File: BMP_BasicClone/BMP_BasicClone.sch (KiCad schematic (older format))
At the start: 53 parts, among them J1 BARREL_JACK, Q1 MMBT3904, Q2 MMBT3904, Q3 MMBT3904, Q4 MMBT3904

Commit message: update
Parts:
- J1: symbol BARREL_JACK -> BARREL_JACK-RESCUE-BMP_BasicClone
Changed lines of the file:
@@
 EESchema Schematic File Version 2
+LIBS:BMP_BasicClone-rescue
 LIBS:power
 LIBS:device
@@
 VOLUME
 $Comp
-L BARREL_JACK J1
+L BARREL_JACK-RESCUE-BMP_BasicClone J1
 U 1 1 5A2DF800
 P 1650 1850

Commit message: updates
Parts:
- R1: value R -> 1k
- SW_EN1: footprint custom_sw:SW_3PDT_W18MM_L17.3MM_P5.3MM_D2MM -> custom_sw:SW_3PDT_W18MM_L17.3MM_P5.3MM_D2MM_SolderLugs
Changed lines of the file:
@@
 F 0 "SW_EN1" H 9850 2700 50  0000 C CNN
 F 1 "SW_3PDT_on_on" H 9800 2750 50  0001 C CNN
-F 2 "custom_sw:SW_3PDT_W18MM_L17.3MM_P5.3MM_D2MM" H 9800 2950 50  0001 C CNN
+F 2 "custom_sw:SW_3PDT_W18MM_L17.3MM_P5.3MM_D2MM_SolderLugs" H 9800 2950 50  0001 C CNN
 F 3 "" H 9800 2950 50  0001 C CNN
 	1    9800 2950
@@
 F 0 "SW_EN1" H 1700 2800 50  0000 C CNN
 F 1 "SW_3PDT_on_on" H 1700 2800 50  0001 C CNN
-F 2 "custom_sw:SW_3PDT_W18MM_L17.3MM_P5.3MM_D2MM" H 1700 3000 50  0001 C CNN
+F 2 "custom_sw:SW_3PDT_W18MM_L17.3MM_P5.3MM_D2MM_SolderLugs" H 1700 3000 50  0001 C CNN
 F 3 "" H 1700 3000 50  0001 C CNN
 	2    1700 3000
@@
 F 0 "SW_EN1" H 1950 6000 50  0000 C CNN
 F 1 "SW_3PDT_on_on" H 1950 6000 50  0001 C CNN
-F 2 "custom_sw:SW_3PDT_W18MM_L17.3MM_P5.3MM_D2MM" H 1950 6200 50  0001 C CNN
+F 2 "custom_sw:SW_3PDT_W18MM_L17.3MM_P5.3MM_D2MM_SolderLugs" H 1950 6200 50  0001 C CNN
 F 3 "" H 1950 6200 50  0001 C CNN
 	3    1950 6200
@@
 P 2850 2900
 F 0 "R1" V 2930 2900 50  0000 C CNN
-F 1 "R" V 2850 2900 50  0000 C CNN
+F 1 "1k" V 2850 2900 50  0000 C CNN
 F 2 "Resistors_SMD:R_0402_NoSilk" V 2780 2900 50  0001 C CNN
 F 3 "" H 2850 2900 50  0001 C CNN

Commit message: update
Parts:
- removed R24, R25, R26: 100K, Potentiometers:Potentiometer_Bourns_PTV09A-1_Horizontal, symbol POT
- added J2, J3: CONN_02X06, Pin_Headers:Pin_Header_Straight_2x06_Pitch2.54mm, symbol CONN_02X06
- added SUSTAIN1, TONE1, VOLUME1: 100K, Potentiometers:Potentiometer_Bourns_PTV09A-1_Horizontal, symbol POT
- C1, C10, C11, C12, C13, C2, C3, C4, C5, C6, C7, C8, C9: footprint Capacitors_SMD:C_0402_NoSilk -> Capacitors_SMD:C_0805
- D1, D2, D3, D4, D6: footprint Diodes_SMD:D_SOD-323_HandSoldering -> Diodes_SMD:D_SOD-523
- R1, R10, R11, R12, R13, R14, R15, R16, R17, R18, R19, R2, R20, R21, R22, R23, R3, R4, R5, R6, R7, R8, R9: footprint Resistors_SMD:R_0402_NoSilk -> Resistors_SMD:R_0805
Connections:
- net GND: now also J2.2 (P2), J2.8 (P8); no longer R1.1
- net SUS_P3: now reaches C4.1
- net SUS_P3: now also J2.7 (P7)
- net SUS_P2: now reaches C5.1
- net SUS_P2: now also J2.9 (P9)
- net SUS_P1: now reaches R23.1
- net SUS_P1: now also J2.11 (P11)
- net TONE_P3: now reaches C9.1, R5.2
- net TONE_P3: now also J2.1 (P1)
- net TONE_P1: now reaches C8.1, R8.1
- net TONE_P1: now also J2.5 (P5)
- net TONE_P2: now reaches C3.2
- net TONE_P2: now also J2.3 (P3)
- net VOL_P1: now reaches C2.2
- net VOL_P1: now also J2.12 (P12)
- net VOL_P2: now reaches SW_EN1.3 (C)
- net VOL_P2: now also J2.10 (P10)
- net at D5.2 (A): now also J3.4 (P4); no longer SW_EN1.6 (C)
- net at D5.1 (K): now also R1.1; no longer R1.2
- new net: J3.2 (P2), R1.2
- new net: J3.1 (P1), TONE1.1
- new net: J3.10 (P10), VOLUME1.2
- new net: J3.11 (P11), SUSTAIN1.3
- new net: J3.12 (P12), VOLUME1.1
- new net: J3.3 (P3), TONE1.2
- new net: J3.5 (P5), TONE1.3
- new net: J3.7 (P7), SUSTAIN1.1
- new net: J3.8 (P8), VOLUME1.3
- new net: J3.9 (P9), SUSTAIN1.2
- new net LED_AN: J2.4 (P4), SW_EN1.6 (C)
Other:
- note removed: "SUSTAIN"
- note removed: "TONE"
- note removed: "VOLUME"
- moved on the sheet: C1, C10, C11, C12, C13, C2, C3, C4, C5, C6, C7, C8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

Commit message: board update
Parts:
- renumbered C9 to C10, C8 to C11, C3 to C12, C2 to C13, C10 to C2, C4 to C3, C5 to C4, C6 to C5, C12 to C6, C13 to C7, C7 to C8, C11 to C9, D6 to D1, D4 to D2, D2 to D4, D1 to D5, D5 to D6, Q4 to Q1, Q3 to Q2, Q2 to Q3, Q1 to Q4, R2 to R1, R18 to R10, R21 to R11, R16 to R13, R15 to R14, R11 to R15, R10 to R16, R8 to R17, R5 to R18, R7 to R19, R14 to R2, R3 to R20, R6 to R21, R4 to R22, R1 to R23, R9 to R3, R13 to R4, R22 to R5, R23 to R6, R19 to R7, R20 to R8, R17 to R9
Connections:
- net +9V: now also SW_EN1.5 (B); no longer SW_EN1.5 (B)
- net LED_AN: now also SW_EN1.6 (C); no longer SW_EN1.6 (C)
- net VOL_P2: now also SW_EN1.1 (A); no longer SW_EN1.3 (C)
- net at R1.2: now also SW_EN1.7 (A); no longer SW_EN1.9 (C)
- net at J_OUT1.1 (TIP): now also SW_EN1.2 (B); no longer SW_EN1.2 (B)
- net at J_IN1.1 (TIP): now also SW_EN1.8 (B); no longer SW_EN1.8 (B)
- new net: SW_EN1.3 (C), SW_EN1.9 (C)

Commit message: Update
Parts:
- removed J2, J3: CONN_02X06, Pin_Headers:Pin_Header_Straight_2x06_Pitch2.54mm, symbol CONN_02X06
- added J_AUX2MAIN_1, J_AUX2MAIN_2, J_MAIN2AUX_1, J_MAIN2AUX_2: CONN_01X06, Pin_Headers:Pin_Header_Straight_1x06_Pitch2.54mm, symbol CONN_01X06
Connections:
- net GND: now also J_MAIN2AUX_2.3 (P3), J_MAIN2AUX_2.6 (P6)
- net LED_AN: now also J_MAIN2AUX_2.5 (P5)
- net SUS_P1: now also J_MAIN2AUX_1.6 (P6)
- net SUS_P2: now also J_MAIN2AUX_1.5 (P5)
- net SUS_P3: now also J_MAIN2AUX_1.4 (P4)
- net TONE_P1: now also J_MAIN2AUX_1.3 (P3)
- net TONE_P2: now also J_MAIN2AUX_1.2 (P2)
- net TONE_P3: now also J_MAIN2AUX_1.1 (P1)
- net VOL_P1: now also J_MAIN2AUX_2.1 (P1)
- net VOL_P2: now also J_MAIN2AUX_2.2 (P2)
- net at D6.2 (A): now also J_AUX2MAIN_2.5 (P5)
- net at R23.2: now also J_AUX2MAIN_2.6 (P6)
- net at TONE1.1: now also J_AUX2MAIN_1.1 (P1)
- net at VOLUME1.2: now also J_AUX2MAIN_2.2 (P2)
- net at SUSTAIN1.3: now also J_AUX2MAIN_1.6 (P6)
- net at VOLUME1.1: now also J_AUX2MAIN_2.1 (P1)
- net at TONE1.2: now also J_AUX2MAIN_1.2 (P2)
- net at TONE1.3: now also J_AUX2MAIN_1.3 (P3)
- net at SUSTAIN1.1: now also J_AUX2MAIN_1.4 (P4)
- net at VOLUME1.3: now also J_AUX2MAIN_2.3 (P3)
- net at SUSTAIN1.2: now also J_AUX2MAIN_1.5 (P5)
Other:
- moved on the sheet: D6, R23, SUSTAIN1, TONE1, VOLUME1
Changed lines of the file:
@@
 L LED D6
 U 1 1 5A2E0726
-P 9200 5750
-F 0 "D6" H 9200 5850 50  0000 C CNN
-F 1 "LED" H 9200 5650 50  0000 C CNN
-F 2 "LEDs:LED_D5.0mm" H 9200 5750 50  0001 C CNN
-F 3 "" H 9200 5750 50  0001 C CNN
-	1    9200 5750
+P 9200 5850
+F 0 "D6" H 9200 5950 50  0000 C CNN
+F 1 "LED" H 9200 5750 50  0000 C CNN
+F 2 "LEDs:LED_D5.0mm" H 9200 5850 50  0001 C CNN
+F 3 "" H 9200 5850 50  0001 C CNN
+	1    9200 5850
 	0    -1   -1   0
 $EndComp
@@
 L R R23
 U 1 1 5A2E81A3
-P 9500 5750
-F 0 "R23" V 9580 5750 50  0000 C CNN
-F 1 "1k" V 9500 5750 50  0000 C CNN
-F 2 "Resistors_SMD:R_0805" V 9430 5750 50  0001 C CNN
-F 3 "" H 9500 5750 50  0001 C CNN
-	1    9500 5750
+P 9500 5850
+F 0 "R23" V 9580 5850 50  0000 C CNN
+F 1 "1k" V 9500 5850 50  0000 C CNN
+F 2 "Resistors_SMD:R_0805" V 9430 5850 50  0001 C CNN
+F 3 "" H 9500 5850 50  0001 C CNN
+	1    9500 5850
 	-1   0    0    1
 $EndComp
@@
 $EndComp
 $Comp
-L CONN_02X06 J3
-U 1 1 5A33F471
-P 9050 5200
-F 0 "J3" H 9050 5550 50  0000 C CNN
-F 1 "CONN_02X06" H 9050 4850 50  0000 C CNN
-F 2 "Pin_Headers:Pin_Header_Straight_2x06_Pitch2.54mm" H 9050 4000 50  0001 C CNN
-F 3 "" H 9050 4000 50  0001 C CNN
-	1    9050 5200
-	0    1    1    0
-$EndComp
-$Comp
 L POT SUSTAIN1
 U 1 1 5A34007A
-P 8750 4350
-F 0 "SUSTAIN1" V 8550 4350 50  0000 C CNN
-F 1 "100K" V 8650 4350 50  0000 C CNN
-F 2 "Potentiometers:Potentiometer_Bourns_PTV09A-1_Horizontal" H 8750 4350 50  0001 C CNN
-F 3 "" H 8750 4350 50  0001 C CNN
-	1    8750 4350
+P 8750 4200
+F 0 "SUSTAIN1" V 8550 4200 50  0000 C CNN
+F 1 "100K" V 8650 4200 50  0000 C CNN
+F 2 "Potentiometers:Potentiometer_Bourns_PTV09A-1_Horizontal" H 8750 4200 50  0001 C CNN
+F 3 "" H 8750 4200 50  0001 C CNN
+	1    8750 4200
 	0    1    1    0
 $EndComp
@@
 Text Label 4250 5400 1    60   ~ 0
 SUS_P2
-$Comp
-L CONN_02X06 J2
-U 1 1 5A342A65
-P 8050 5200
-F 0 "J2" H 8050 5550 50  0000 C CNN
-F 1 "CONN_02X06" H 8050 4850 50  0000 C CNN
-F 2 "Pin_Headers:Pin_Header_Straight_2x06_Pitch2.54mm" H 8050 4000 50  0001 C CNN
-F 3 "" H 8050 4000 50  0001 C CNN
-	1    8050 5200
-	0    1    1    0
-$EndComp
-Text Label 7800 4550 3    60   ~ 0
+Text Label 7650 4400 3    60   ~ 0
 SUS_P1
-Text Label 7900 4550 3    60   ~ 0
+Text Label 7750 4400 3    60   ~ 0
 SUS_P2
-Text Label 8000 4550 3    60   ~ 0
+Text Label 7850 4400 3    60   ~ 0
 SUS_P3
 $Comp
 L POT TONE1
 U 1 1 5A3434FD
-P 9350 4350
-F 0 "TONE1" V 9150 4350 50  0000 C CNN
-F 1 "100K" V 9250 4350 50  0000 C CNN
-F 2 "Potentiometers:Potentiometer_Bourns_PTV09A-1_Horizontal" H 9350 4350 50  0001 C CNN
-F 3 "" H 9350 4350 50  0001 C CNN
-	1    9350 4350
+P 9350 4200
+F 0 "TONE1" V 9150 4200 50  0000 C CNN
+F 1 "100K" V 9250 4200 50  0000 C CNN
+F 2 "Potentiometers:Potentiometer_Bourns_PTV09A-1_Horizontal" H 9350 4200 50  0001 C CNN
+F 3 "" H 9350 4200 50  0001 C CNN
+	1    9350 4200
 	0    1    1    0
 $EndComp
-Text Label 8100 4550 3    60   ~ 0
+Text Label 7950 4400 3    60   ~ 0
 TONE_P1
-Text Label 8200 4550 3    60   ~ 0
+Text Label 8050 4400 3    60   ~ 0
 TONE_P2
-Text Label 8300 4550 3    60   ~ 0
+Text Label 8150 4400 3    60   ~ 0
 TONE_P3
 Text Label 7550 2400 3    60   ~ 0
@@
 Text Label 7400 2250 0    60   ~ 0
 TONE_P2
-Text Label 7800 5850 1    60   ~ 0
+Text Label 7650 5950 1    60   ~ 0
 VOL_P1
-Text Label 7900 5850 1    60   ~ 0
+Text Label 7750 5950 1    60   ~ 0
 VOL_P2
-Text Label 8000 5850 1    60   ~ 0
+Text Label 7850 5950 1    60   ~ 0
 VOL_P3
-Text Label 8200 5850 1    60   ~ 0
+Text Label 8050 5950 1    60   ~ 0
 LED_AN
-Text Label 8300 5850 1    60   ~ 0
+Text Label 8150 5950 1    60   ~ 0
 LED_CA
 $Comp
 L POT VOLUME1
 U 1 1 5A346136
-P 8750 6000
-F 0 "VOLUME1" V 8550 6000 50  0000 C CNN
-F 1 "100K" V 8650 6000 50  0000 C CNN
-F 2 "Potentiometers:Potentiometer_Bourns_PTV09A-1_Horizontal" H 8750 6000 50  0001 C CNN
-F 3 "" H 8750 6000 50  0001 C CNN
-	1    8750 6000
+P 8750 6100
+F 0 "VOLUME1" V 8550 6100 50  0000 C CNN
+F 1 "100K" V 8650 6100 50  0000 C CNN
+F 2 "Potentiometers:Potentiometer_Bourns_PTV09A-1_Horizontal" H 8750 6100 50  0001 C CNN
+F 3 "" H 8750 6100 50  0001 C CNN
+	1    8750 6100
 	0    -1   -1   0
 $EndComp
@@
 VOL_P3
 Wire Wire Line
-	9300 5500 9300 5450
-Wire Wire Line
-	9500 5500 9300 5500
-Wire Wire Line
-	9500 5600 9500 5500
-Wire Wire Line
-	9500 6050 9500 5900
-Wire Wire Line
-	9200 6050 9500 6050
-Wire Wire Line
-	9200 5900 9200 6050
-Wire Wire Line
-	9200 5600 9200 5450
-Wire Wire Line
-	8800 5550 8800 5450
-Wire Wire Line
-	8550 5550 8800 5550
-Wire Wire Line
-	8550 6000 8550 5550
-Wire Wire Line
-	8600 6000 8550 6000
-Wire Wire Line
-	8900 5650 8900 5450
-Wire Wire Line
-	8750 5650 8900 5650
-Wire Wire Line
-	8750 5850 8750 5650
-Wire Wire Line
-	9000 6000 9000 5450
-Wire Wire Line
-	8900 6000 9000 6000
-Wire Wire Line
-	8200 5450 8200 5850
-Wire Wire Line
-	8300 5450 8300 5850
-Wire Wire Line
-	8000 5450 8000 5850
-Wire Wire Line
-	7900 5450 7900 5850
-Wire Wire Line
-	7800 5450 7800 5850
-Wire Wire Line
-	8300 4950 8300 4550
-Wire Wire Line
-	8200 4550 8200 4950
-Wire Wire Line
-	8100 4550 8100 4950
-Wire Wire Line
-	9550 4350 9500 4350
-Wire Wire Line
-	9550 4850 9550 4350
-Wire Wire Line
-	9300 4850 9550 4850
-Wire Wire Line
-	9300 4950 9300 4850
-Wire Wire Line
-	9200 4800 9200 4950
-Wire Wire Line
-	9350 4800 9200 4800
-Wire Wire Line
-	9350 4500 9350 4800
-Wire Wire Line
-	9100 4350 9100 4950
-Wire Wire Line
-	9200 4350 9100 4350
-Wire Wire Line
-	8000 4950 8000 4550
-Wire Wire Line
-	7900 4550 7900 4950
-Wire Wire Line
-	7800 4950 7800 4550
-Wire Wire Line
-	8900 4800 8750 4800
-Wire Wire Line
-	8900 4950 8900 4800
-Wire Wire Line
-	8750 4800 8750 4500
-Wire Wire Line
-	8550 4350 8600 4350
-Wire Wire Line
-	8550 4850 8550 4350
-Wire Wire Line
-	8800 4850 8550 4850
-Wire Wire Line
-	8800 4950 8800 4850
-Wire Wire Line
-	9000 4350 9000 4950
-Wire Wire Line
-	8900 4350 9000 4350
+	9300 5600 9300 5550
+Wire Wire Line
+	9500 5600 9300 5600
+Wire Wire Line
+	9500 5700 9500 5600
+Wire Wire Line
+	9500 6150 9500 6000
+Wire Wire Line
+	9200 6150 9500 6150
+Wire Wire Line
+	9200 6000 9200 6150
+Wire Wire Line
+	9200 5700 9200 5550
+Wire Wire Line
+	8800 5650 8800 5550
+Wire Wire Line
+	8550 5650 8800 5650
+Wire Wire Line
+	8550 6100 8550 5650
+Wire Wire Line
+	8600 6100 8550 6100
+Wire Wire Line
+	8900 5750 8900 5550
+Wire Wire Line
+	8750 5750 8900 5750
+Wire Wire Line
+	8750 5950 8750 5750
+Wire Wire Line
+	9000 6100 9000 5550
+Wire Wire Line
+	8900 6100 9000 6100
+Wire Wire Line
+	8050 5550 8050 5950
+Wire Wire Line
+	8150 5550 8150 5950
+Wire Wire Line
+	7850 5550 7850 5950
+Wire Wire Line
+	7750 5550 7750 5950
+Wire Wire Line
+	7650 5550 7650 5950
+Wire Wire Line
+	8150 4800 8150 4400
+Wire Wire Line
+	8050 4400 8050 4800
+Wire Wire Line
+	7950 4400 7950 4800
+Wire Wire Line
+	9550 4200 9500 4200
+Wire Wire Line
+	9550 4700 9550 4200
+Wire Wire Line
+	9300 4700 9550 4700
+Wire Wire Line
+	9300 4800 9300 4700
+Wire Wire Line
+	9200 4650 9200 4800
+Wire Wire Line
+	9350 4650 9200 4650
+Wire Wire Line
+	9350 4350 9350 4650
+Wire Wire Line
+	9100 4200 9100 4800
+Wire Wire Line
+	9200 4200 9100 4200
+Wire Wire Line
+	7850 4800 7850 4400
+Wire Wire Line
+	7750 4400 7750 4800
+Wire Wire Line
+	7650 4800 7650 4400
+Wire Wire Line
+	8900 4650 8750 4650
+Wire Wire Line
+	8900 4800 8900 4650
+Wire Wire Line
+	8750 4650 8750 4350
+Wire Wire Line
+	8550 4200 8600 4200
+Wire Wire Line
+	8550 4700 8550 4200
+Wire Wire Line
+	8800 4700 8550 4700
+Wire Wire Line
+	8800 4800 8800 4700
+Wire Wire Line
+	9000 4200 9000 4800
+Wire Wire Line
+	8900 4200 9000 4200
 Connection ~ 6850 1950
 Wire Wire Line
@@
 Wire Wire Line
 	6300 3800 6300 6550
+$Comp
+L CONN_01X06 J_MAIN2AUX_1
+U 1 1 5A3EEED2
+P 7900 5000
+F 0 "J_MAIN2AUX_1" V 8000 5000 50  0000 C CNN
+F 1 "CONN_01X06" V 8000 5000 50  0001 C CNN
+F 2 "Pin_Headers:Pin_Header_Straight_1x06_Pitch2.54mm" H 7900 5000 50  0001 C CNN
+F 3 "" H 7900 5000 50  0001 C CNN
+	1    7900 5000
+	0    1    1    0
+$EndComp
+$Comp
+L CONN_01X06 J_MAIN2AUX_2
+U 1 1 5A3EEFA8
+P 7900 5350
+F 0 "J_MAIN2AUX_2" V 8000 5350 50  0000 C CNN
+F 1 "CONN_01X06" V 8000 5350 50  0001 C CNN
+F 2 "Pin_Headers:Pin_Header_Straight_1x06_Pitch2.54mm" H 7900 5350 50  0001 C CNN
+F 3 "" H 7900 5350 50  0001 C CNN
+	1    7900 5350
+	0    -1   -1   0
+$EndComp
+$Comp
+L CONN_01X06 J_AUX2MAIN_1
+U 1 1 5A3F0090
+P 9050 5000
+F 0 "J_AUX2MAIN_1" V 9150 5000 50  0000 C CNN
+F 1 "CONN_01X06" V 9150 5000 50  0001 C CNN
+F 2 "Pin_Headers:Pin_Header_Straight_1x06_Pitch2.54mm" H 9050 5000 50  0001 C CNN
+F 3 "" H 9050 5000 50  0001 C CNN
+	1    9050 5000
+	0    1    1    0
+$EndComp
+$Comp
+L CONN_01X06 J_AUX2MAIN_2
+U 1 1 5A3F0164
+P 9050 5350
+F 0 "J_AUX2MAIN_2" V 9150 5350 50  0000 C CNN
+F 1 "CONN_01X06" V 9150 5350 50  0001 C CNN
+F 2 "Pin_Headers:Pin_Header_Straight_1x06_Pitch2.54mm" H 9050 5350 50  0001 C CNN
+F 3 "" H 9050 5350 50  0001 C CNN
+	1    9050 5350
+	0    -1   -1   0
+$EndComp
 $EndSCHEMATC

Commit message: Updates
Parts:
- C1, C10, C11, C12, C13, C2, C3, C4, C5, C6, C7, C8, C9: footprint Capacitors_SMD:C_0805 -> Capacitors_SMD:C_0805_HandSoldering
- D1, D2, D3, D4, D5: footprint Diodes_SMD:D_SOD-523 -> Diodes_SMD:D_SOD-323
- R1, R10, R11, R12, R13, R14, R15, R16, R17, R18, R19, R2, R20, R21, R22, R23, R3, R4, R5, R6, R7, R8, R9: footprint Resistors_SMD:R_0805 -> Resistors_SMD:R_0805_HandSoldering
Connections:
- net LED_AN: now also SW_EN1.4 (A); no longer SW_EN1.6 (C)

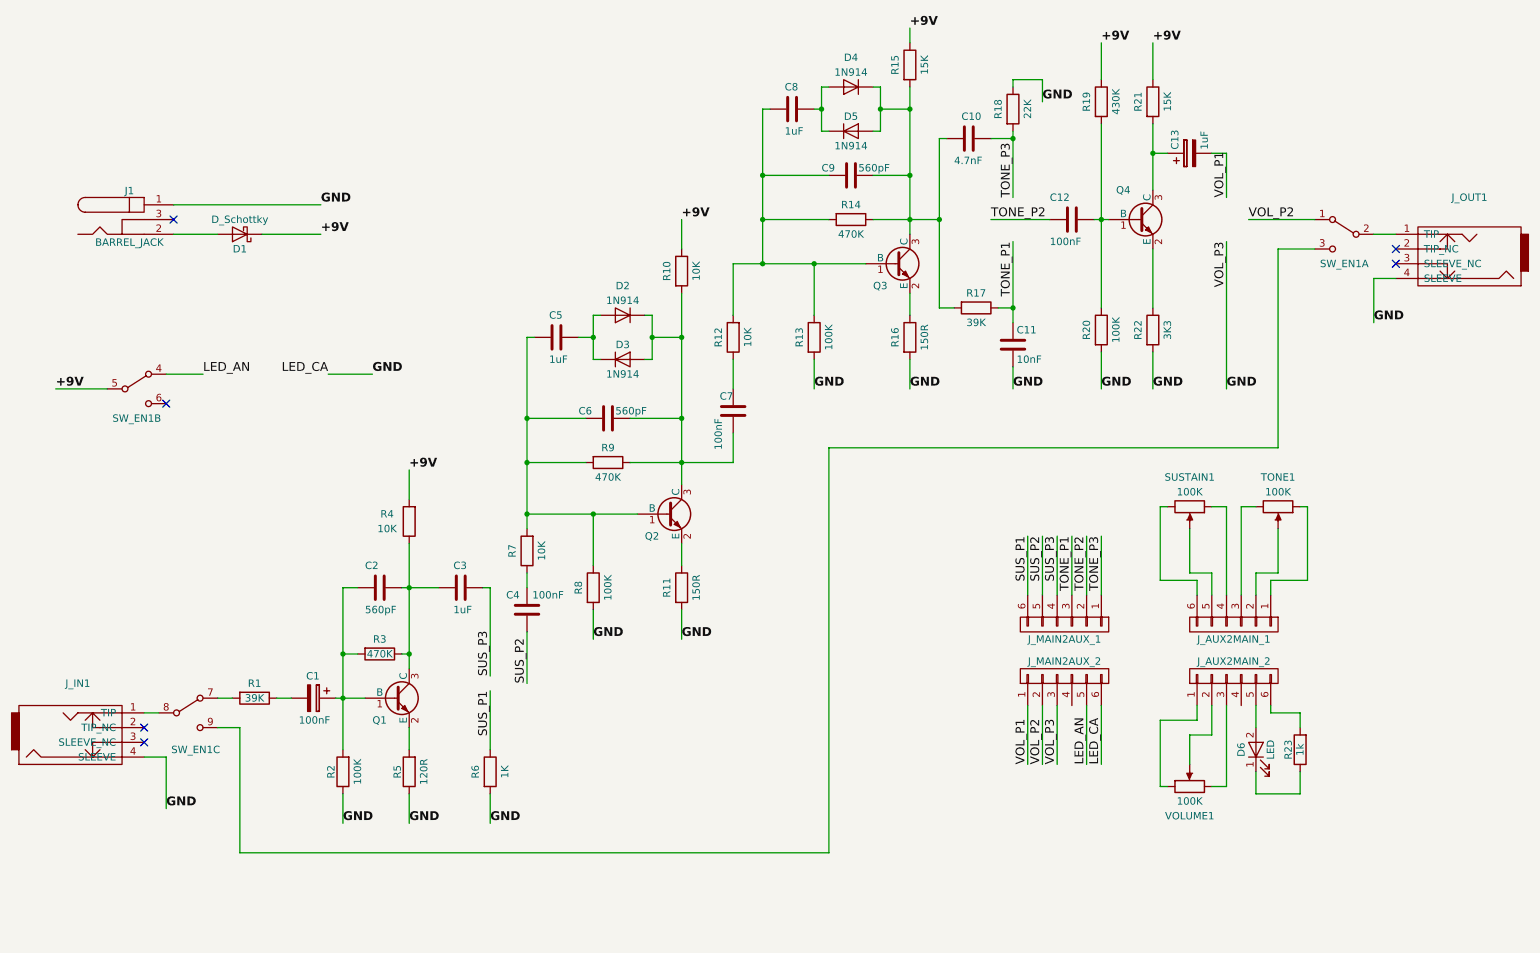
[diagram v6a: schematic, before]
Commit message: Added SuperCollider Schema and Layout
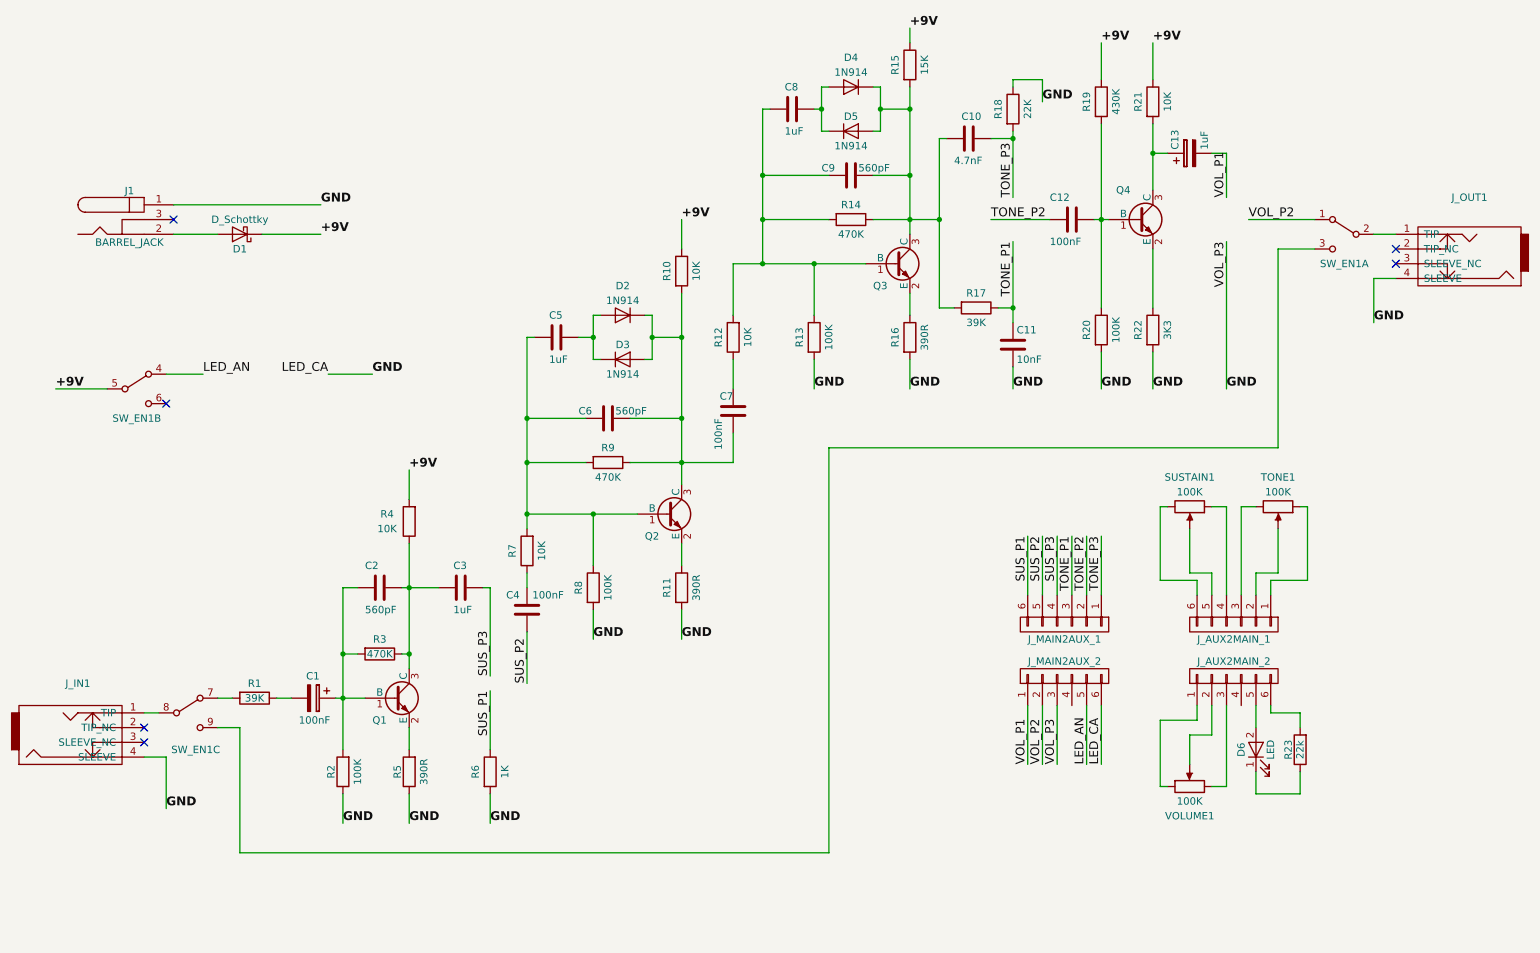
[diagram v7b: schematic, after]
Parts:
- R11, R16: value 150R -> 390R
- R21: value 15K -> 10K
- R23: value 1k -> 22k
- R5: value 120R -> 390R
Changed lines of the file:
@@
 P 3450 6000
 F 0 "R5" V 3530 6000 50  0000 C CNN
-F 1 "120R" V 3350 6000 50  0000 C CNN
+F 1 "390R" V 3350 6000 50  0000 C CNN
 F 2 "Resistors_SMD:R_0805_HandSoldering" V 3380 6000 50  0001 C CNN
 F 3 "" H 3450 6000 50  0001 C CNN
@@
 P 5300 4750
 F 0 "R11" V 5200 4750 50  0000 C CNN
-F 1 "150R" V 5400 4750 50  0000 C CNN
+F 1 "390R" V 5400 4750 50  0000 C CNN
 F 2 "Resistors_SMD:R_0805_HandSoldering" V 5230 4750 50  0001 C CNN
 F 3 "" H 5300 4750 50  0001 C CNN
@@
 P 6850 3050
 F 0 "R16" V 6750 3050 50  0000 C CNN
-F 1 "150R" V 6950 3050 50  0000 C CNN
+F 1 "390R" V 6950 3050 50  0000 C CNN
 F 2 "Resistors_SMD:R_0805_HandSoldering" V 6780 3050 50  0001 C CNN
 F 3 "" H 6850 3050 50  0001 C CNN
@@
 P 8500 1450
 F 0 "R21" V 8400 1450 50  0000 C CNN
-F 1 "15K" V 8600 1450 50  0000 C CNN
+F 1 "10K" V 8600 1450 50  0000 C CNN
 F 2 "Resistors_SMD:R_0805_HandSoldering" V 8430 1450 50  0001 C CNN
 F 3 "" H 8500 1450 50  0001 C CNN
@@
 P 9500 5850
 F 0 "R23" V 9580 5850 50  0000 C CNN
-F 1 "1k" V 9500 5850 50  0000 C CNN
+F 1 "22k" V 9500 5850 50  0000 C CNN
 F 2 "Resistors_SMD:R_0805_HandSoldering" V 9430 5850 50  0001 C CNN
 F 3 "" H 9500 5850 50  0001 C CNN
